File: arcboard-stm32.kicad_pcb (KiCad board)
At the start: 2 copper layers, 59.5 x 59.7 mm, 91 parts, among them J1 Conn_01x04_Socket, J10 Conn_01x04_Socket, J11 Conn_01x02_Socket, J12 Conn_01x03_Socket, J13 FFC05001-12SBA124W5M, J14 FFC05001-12SBA124W5M, J15 FFC05001-12SBA124W5M, J16 FFC05001-12SBA124W5M, J17 Conn_01x04_Socket, J2 Conn_01x04_Socket, J3 FFC05001-12SBA124W5M, J4 FFC05001-12SBA124W5M, J5 Conn_01x02_Socket, J6 FFC05001-12SBA124W5M, J7 FFC05001-12SBA124W5M, J8 FFC05001-12SBA124W5M, J9 Conn_01x03_Socket, U1 XC6210B332MR-G, U10 1N4148W_C81598, U13 2N7002, U14 W25Q128JVSIQTR, U15 TS-1187A-B-A-B, U3 STM32F405RGTx, U4 2N7002, U5 BAV70S,115, U6 BAV70S,115, U7 BAV70S,115, U8 BAV70S,115, U9 BAV70S,115, Y1 Crystal_GND24

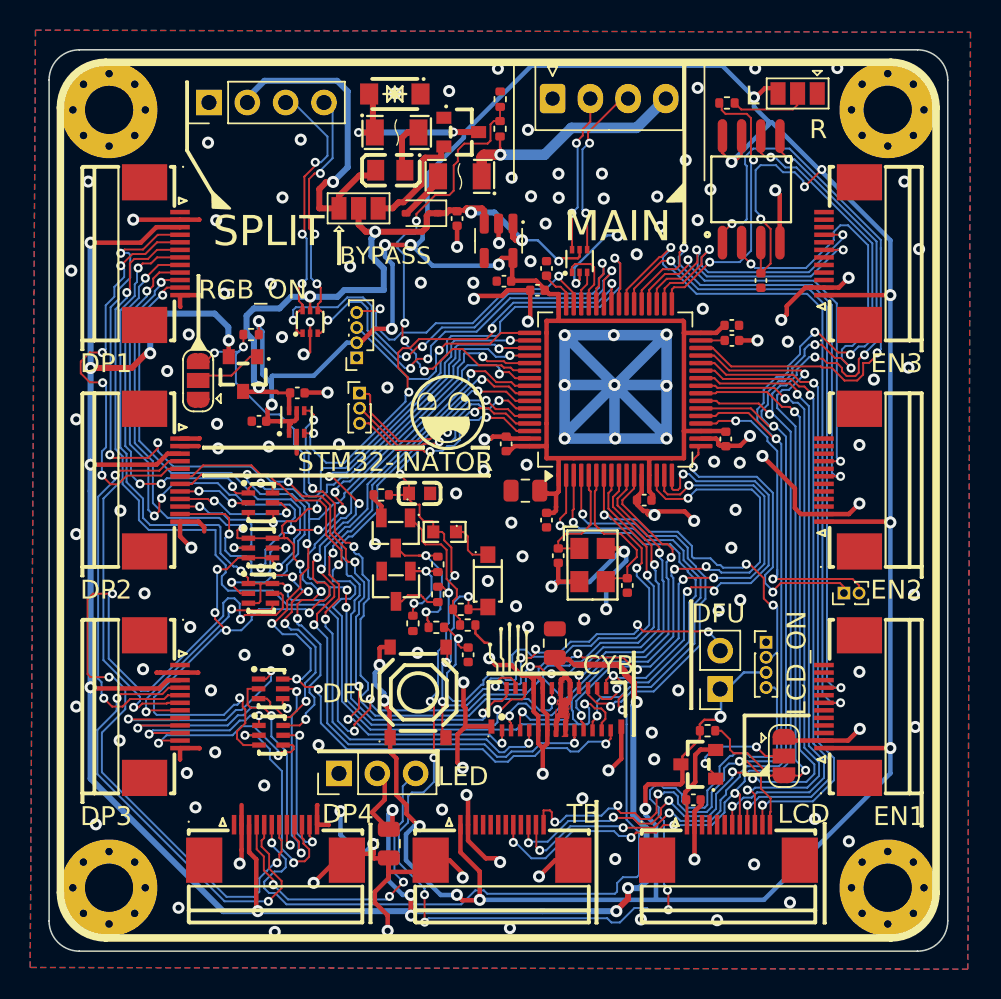
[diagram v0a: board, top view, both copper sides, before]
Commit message: fixing bad mosfet configuration, changing crystal to 12mhz
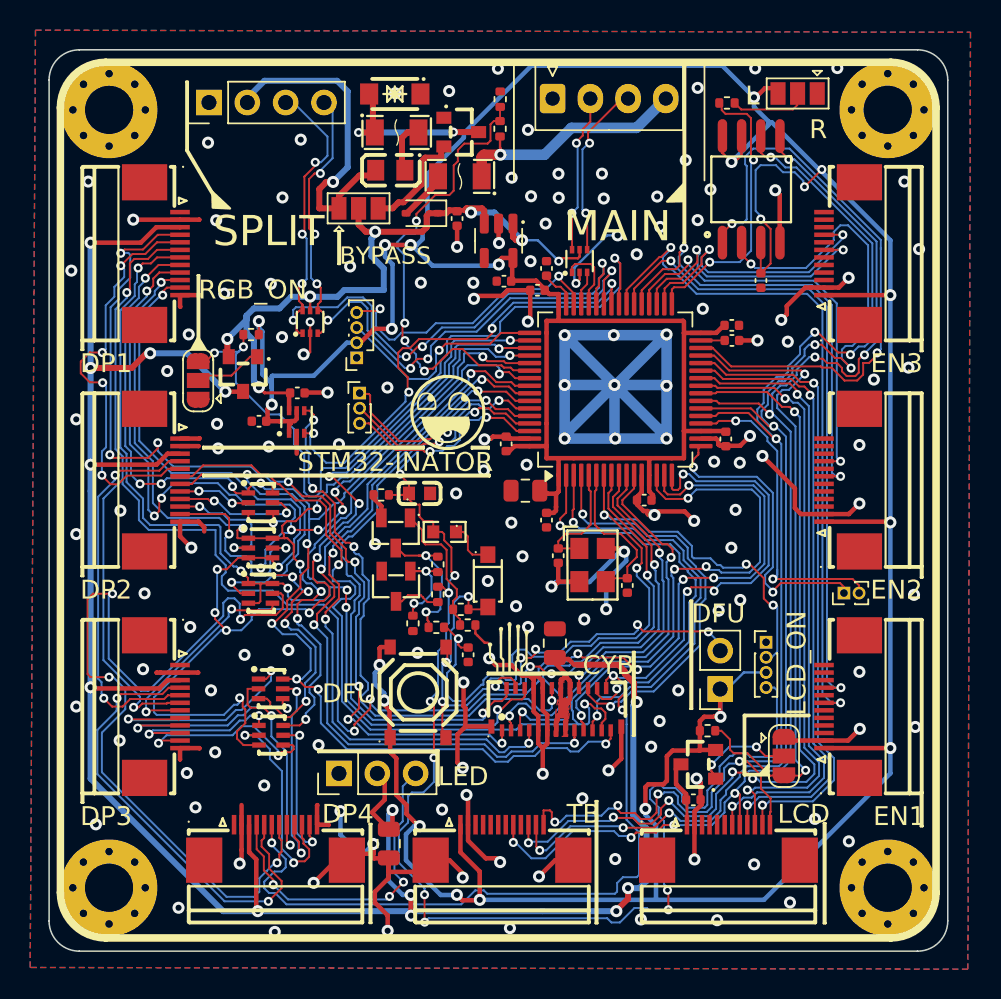
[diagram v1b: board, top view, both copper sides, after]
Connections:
- MOSFET2 pad 2: RGB_5V -> +5V
- MOSFET2 pad 3: +5V -> RGB_5V
- MOSFET3 pad 2: LCD_3V3 -> +3V3
- MOSFET3 pad 3: +3V3 -> LCD_3V3
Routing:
- net +3V3: track 295.5 -> 299.6 mm
- net RGB_5V: track 161.9 -> 159.5 mm
- net +5V: track 47.6 -> 49.9 mm, vias 6 -> 7
- net LCD_3V3: track 6.55 -> 4.46 mm
- net GND: track 222.3 -> 223.8 mm, vias 148 -> 149
- net Net-(JP4-C): track 7.65 -> 6.72 mm
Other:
- board text added: "mk20-v1.1"
- board text removed: "mk20-v1.0"
